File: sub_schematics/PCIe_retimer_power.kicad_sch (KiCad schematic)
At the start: 49 parts

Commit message: Added capacitors
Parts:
- removed C?: C, symbol Device:C
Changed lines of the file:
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@@
 	(wire
 		(pts
-			(xy 31.75 180.34) (xy 21.59 180.34)
-		)
-		(stroke
-			(width 0)
-			(type default)
-		)
-	)
-	(wire
-		(pts
 			(xy 19.05 77.47) (xy 19.05 87.63)
 		)
@@
 	(wire
 		(pts
-			(xy 31.75 167.64) (xy 21.59 167.64)
-		)
-		(stroke
-			(width 0)
-			(type default)
-		)
-	)
-	(wire
-		(pts
 			(xy 115.57 152.4) (xy 115.57 156.21)
 		)
@@
 	(wire
 		(pts
-			(xy 21.59 167.64) (xy 21.59 170.18)
-		)
-		(stroke
-			(width 0)
-			(type default)
-		)
-	)
-	(wire
-		(pts
 			(xy 64.77 154.94) (xy 62.23 154.94)
 		)
@@
 	(wire
 		(pts
-			(xy 21.59 177.8) (xy 21.59 180.34)
-		)
-		(stroke
-			(width 0)
-			(type default)
-		)
-	)
-	(wire
-		(pts
 			(xy 203.2 49.53) (xy 203.2 52.07)
 		)
@@
 					(unit 1)
 				)
-			)
-		)
-	)
-	(symbol
-		(lib_id "Device:C")
-		(at 21.59 173.99 0)
-		(unit 1)
-		(body_style 1)
-		(exclude_from_sim no)
-		(in_bom yes)
-		(on_board yes)
-		(in_pos_files yes)
-		(dnp no)
-		(fields_autoplaced yes)
-		(property "Reference" "C?"
-			(at 25.4 172.7199 0)
-			(show_name no)
-			(do_not_autoplace no)
-			(effects
-				(font
-					(size 1.27 1.27)
-				)
-				(justify left)
-			)
-		)
-		(property "Value" "C"
-			(at 25.4 175.2599 0)
-			(show_name no)
-			(do_not_autoplace no)
-			(effects
-				(font
-					(size 1.27 1.27)
-				)
-				(justify left)
-			)
-		)
-		(property "Footprint" ""
-			(at 22.5552 177.8 0)
-			(hide yes)
-			(show_name no)
-			(do_not_autoplace no)
-			(effects
-				(font
-					(size 1.27 1.27)
-				)
-			)
-		)
-		(property "Datasheet" ""
-			(at 21.59 173.99 0)
-			(hide yes)
-			(show_name no)
-			(do_not_autoplace no)
-			(effects
-				(font
-					(size 1.27 1.27)
-				)
-			)
-		)
-		(property "Description" "Unpolarized capacitor"
-			(at 21.59 173.99 0)
-			(hide yes)
-			(show_name no)
-			(do_not_autoplace no)
-			(effects
-				(font
-					(size 1.27 1.27)
-				)
-			)
-		)
-		(pin "2"
-		)
-		(pin "1"
-		)
-		(instances
-			(project "fw16_MCIO8i"
-				(path "/50f5fd03-67f8-43d1-8bfe-dca2cf908bf0/b129293c-459e-48f0-b955-fe94d8ad35a8/c30304df-3fc6-4616-b0bb-4ddaf654a20e"
-					(reference "C?")
-					(unit 1)
-				)

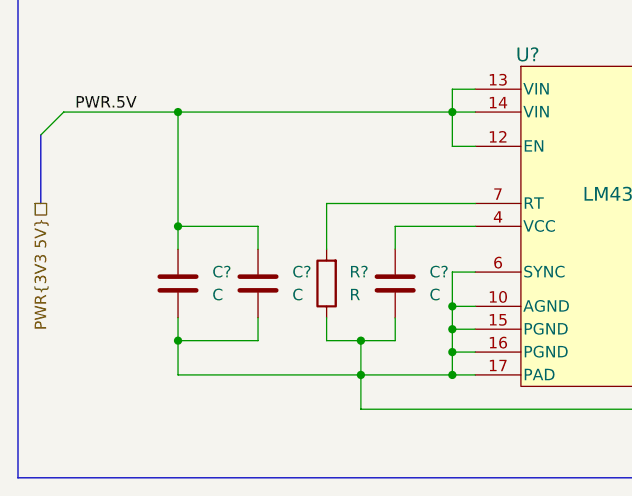
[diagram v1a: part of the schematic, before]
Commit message: Fixed typo
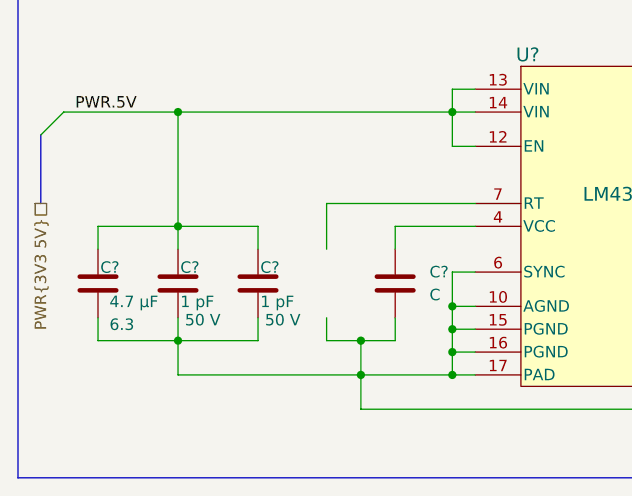
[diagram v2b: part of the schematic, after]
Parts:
- removed C? (x2): C, symbol Device:C
- removed R?: R, symbol Device:R
- added C? (x2): 0402_885392005006, Capacitor_SMD_Wurth:C_Wurth_WCAP-CSRF-0402, symbol WE_WCAP-CSRF:0402_885392005006
- added C?: 0402_885012105008, Capacitor_SMD_Wurth:C_Wurth_WCAP-CSGP-0402, symbol WE_WCAP-CSGP:0402_885012105008
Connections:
- net GND: now also C?.2, C?.2, C?.2
- net PWR.5V: now also C?.1, C?.1, C?.1

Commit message: Working buck converter
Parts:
- removed C? (x20): C, symbol Device:C
- removed C? (x12): C_Polarized_US, symbol Device:C_Polarized_US
- removed L? (x3): L_Small, symbol Device:L_Small
- removed R? (x8): R, symbol Device:R
- added C? (x2): 0402_885012205013, Capacitor_SMD_Wurth:C_Wurth_WCAP-CSGP-0402, symbol WE_WCAP-CSGP:0402_885012205013
- added C? (x10): 1206_H1.6_885012108012, Capacitor_SMD_Wurth:C_Wurth_WCAP-CSGP-1206_H1.6, symbol WE_WCAP-CSGP:1206_H1.6_885012108012
- added C? (x2): 1210_H2.0_885012209005, Capacitor_SMD_Wurth:C_Wurth_WCAP-CSGP-1210_H2.0, symbol WE_WCAP-CSGP:1210_H2.0_885012209005
- added C?: 0603_R_885012006001, Capacitor_SMD_Wurth:C_Wurth_WCAP-CSGP-0603_R, symbol WE_WCAP-CSGP:0603_R_885012006001
- added C? (x4): 1206_H0.8_885012008001, Capacitor_SMD_Wurth:C_Wurth_WCAP-CSGP-1206_H0.8, symbol WE_WCAP-CSGP:1206_H0.8_885012008001
- added C?: 1210_H1.25_885012209003, Capacitor_SMD_Wurth:C_Wurth_WCAP-CSGP-1210_H1.25, symbol WE_WCAP-CSGP:1210_H1.25_885012209003
- added C? (x2): 0402_885012205018, Capacitor_SMD_Wurth:C_Wurth_WCAP-CSGP-0402, symbol WE_WCAP-CSGP:0402_885012205018
- added C?: 0603_R_885012106004, Capacitor_SMD_Wurth:C_Wurth_WCAP-CSGP-0603_R, symbol WE_WCAP-CSGP:0603_R_885012106004
- added C?: 0201_885392004008, Capacitor_SMD_Wurth:C_Wurth_WCAP-CSRF-0201, symbol WE_WCAP-CSRF:0201_885392004008
- added C? (x2): 0201_885012104002, Capacitor_SMD_Wurth:C_Wurth_WCAP-CSGP-0201, symbol WE_WCAP-CSGP:0201_885012104002
- added C? (x2): L7.3W4.3H1.9_875046219001, resistor_rf_alu:CP_Wurth_WCAP-PHSE-L7.3W4.3H1.9, symbol WE_WCAP-PHSE:L7.3W4.3H1.9_875046219001
- added C?: 0402_885012205017, Capacitor_SMD_Wurth:C_Wurth_WCAP-CSGP-0402, symbol WE_WCAP-CSGP:0402_885012205017
- added C?: 0402_885012105004, Capacitor_SMD_Wurth:C_Wurth_WCAP-CSGP-0402, symbol WE_WCAP-CSGP:0402_885012105004
- added C?: 0603_R_885012206021, Capacitor_SMD_Wurth:C_Wurth_WCAP-CSGP-0603_R, symbol WE_WCAP-CSGP:0603_R_885012206021
- added L? (x2): 1510_74439370150, Inductor_SMD_Wurth:L_Wurth_WE-XHMI-1510, symbol WE-XHMI:1510_74439370150
- added L?: 353220_74479335329247, Inductor_SMD_Wurth:L_Wurth_WE-PMFI-353220, symbol WE-PMFI:353220_74479335329247
- added R? (x2): 1210_R_560112140002, Resistor_SMD_Wurth:R_Wurth_WRIS-RSKS-1210_R, symbol WE_WRIS-RSKS:1210_R_560112140002
- added R?: 0603_R_560112116028, Resistor_SMD_Wurth:R_Wurth_WRIS-RSKS-0603_R, symbol WE_WRIS-RSKS:0603_R_560112116028
- added R?: 0402_560112110151, Resistor_SMD_Wurth:R_Wurth_WRIS-RSKS-0402, symbol WE_WRIS-RSKS:0402_560112110151
- added R?: 0402_560112110215, Resistor_SMD_Wurth:R_Wurth_WRIS-RSKS-0402, symbol WE_WRIS-RSKS:0402_560112110215
- added R?: 0402_560112110130, Resistor_SMD_Wurth:R_Wurth_WRIS-RSKS-0402, symbol WE_WRIS-RSKS:0402_560112110130
- added R?: 0603_R_560112116076, Resistor_SMD_Wurth:R_Wurth_WRIS-RSKS-0603_R, symbol WE_WRIS-RSKS:0603_R_560112116076
- added R?: 0603_R_560112116074, Resistor_SMD_Wurth:R_Wurth_WRIS-RSKS-0603_R, symbol WE_WRIS-RSKS:0603_R_560112116074
- added R?: 0603_R_560112116007, Resistor_SMD_Wurth:R_Wurth_WRIS-RSKS-0603_R, symbol WE_WRIS-RSKS:0603_R_560112116007
- added R?: 0402_560112110012, Resistor_SMD_Wurth:R_Wurth_WRIS-RSKS-0402, symbol WE_WRIS-RSKS:0402_560112110012
- C?: Voltage 6.3 -> 6.3 V
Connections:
- net GND: now also C?.2, C?.2, C?.2, C?.2, C?.2, C?.2, C?.2, C?.2, C?.2, C?.2, C?.2, C?.2, C?.2, C?.2, C?.2, C?.2, C?.2, C?.2, C?.2, C?.2, C?.2, R?.1, R?.1, R?.1, R?.2, R?.2, R?.2
- net PWR.1_17V: now also C?.1, C?.1, C?.1, C?.1, C?.1, C?.1, C?.1, C?.1, C?.1, C?.1, C?.1, C?.1, C?.1, C?.1, L?.2, L?.2, R?.1
- net PWR.1_8V: now also C?.1, C?.1, C?.1, L?.2, R?.2
- net PWR.5V: now also C?.1, C?.1, C?.1, C?.1, C?.1, C?.1
- net at U?.18 (FB2_SS): now also C?.1
- net at U?.3 (CBOOT): now also C?.1
- net at U?.1 (SW), U?.2 (SW): now also C?.2, L?.1
- net at U?.11 (PG1_MODE): now also R?.1
- net at U?.14 (FB1): now also R?.1
- net at U?.15 (VCC): now also C?.1, R?.2
- net at U?.17 (RT): now also R?.2
- net at U?.19 (VOSNS2_COMP): now also C?.1, R?.1
- net at U?.2 (CB2): now also C?.1
- net at U?.21 (CONFIG): now also R?.2
- net at U?.3 (SW2): now also C?.2, L?.1
- net at U?.5 (SW1): now also C?.2, L?.1
- net at U?.6 (CB1): now also C?.1
- net at U?.9 (FB): now also C?.2, R?.1, R?.2
- net at U?.4 (VCC): now also C?.1
- net at U?.7 (RT): now also R?.2
- new net: C?.1, R?.2
- new net: C?.2, C?.2, C?.2, C?.2, C?.2, C?.2
- new net: R?.1, R?.1
- no-connect marks 0 -> 2

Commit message: Footprint
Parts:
- removed C? (x9): 1206_H1.6_885012108012, Capacitor_SMD_Wurth:C_Wurth_WCAP-CSGP-1206_H1.6, symbol WE_WCAP-CSGP:1206_H1.6_885012108012
- removed C?: 1210_H2.0_885012209005, Capacitor_SMD_Wurth:C_Wurth_WCAP-CSGP-1210_H2.0, symbol WE_WCAP-CSGP:1210_H2.0_885012209005
- removed L? (x2): 1510_74439370150, Inductor_SMD_Wurth:L_Wurth_WE-XHMI-1510, symbol WE-XHMI:1510_74439370150
- removed R? (x2): 1210_R_560112140002, Resistor_SMD_Wurth:R_Wurth_WRIS-RSKS-1210_R, symbol WE_WRIS-RSKS:1210_R_560112140002
- removed R?: 0603_R_560112116076, Resistor_SMD_Wurth:R_Wurth_WRIS-RSKS-0603_R, symbol WE_WRIS-RSKS:0603_R_560112116076
- added C24: 1210_H2.0_885012209005, WE_WCAP-CSGP:C_Wurth_WCAP-CSGP-1210_H2.0, symbol WE_WCAP-CSGP:1210_H2.0_885012209005
- added C26, C27, C28, C29, C30, C31, C32, C33, C34: 1206_H1.6_885012108012, WE_WCAP-CSGP:C_Wurth_WCAP-CSGP-1206_H1.6, symbol WE_WCAP-CSGP:1206_H1.6_885012108012
- added L2, L3: 353220_74479335329210, WE-PMFI:L_Wurth_WE-PMFI-353220, symbol WE-PMFI:353220_74479335329210
- added R1, R20: 0402_560112110019, WE_WRIS-RSKS:R_Wurth_WRIS-RSKS-0402, symbol WE_WRIS-RSKS:0402_560112110019
- added R17: 0603_R_560112116074, WE_WRIS-RSKS:R_Wurth_WRIS-RSKS-0603_R, symbol WE_WRIS-RSKS:0603_R_560112116074
- C1, C12, C13, C14, C15, C16, C21: renamed from C?; footprint Capacitor_SMD_Wurth:C_Wurth_WCAP-CSGP-0402 -> WE_WCAP-CSGP:C_Wurth_WCAP-CSGP-0402
- C10, C8: renamed from C?; footprint Capacitor_SMD_Wurth:C_Wurth_WCAP-CSRF-0402 -> WE_WCAP-CSRF:C_Wurth_WCAP-CSRF-0402
- C11: renamed from C?; footprint Capacitor_SMD_Wurth:C_Wurth_WCAP-CSGP-0603_R -> WE_WCAP-CSGP:C_Wurth_WCAP-CSGP-0603_R; Voltage 6.3 -> 6.3 V
- C17, C19: renamed from C?; footprint Capacitor_SMD_Wurth:C_Wurth_WCAP-CSGP-0603_R -> WE_WCAP-CSGP:C_Wurth_WCAP-CSGP-0603_R
- C18: renamed from C?; footprint Capacitor_SMD_Wurth:C_Wurth_WCAP-CSRF-0201 -> WE_WCAP-CSRF:C_Wurth_WCAP-CSRF-0201; Voltage 25 -> 25 V
- C2, C3: renamed from C?; footprint Capacitor_SMD_Wurth:C_Wurth_WCAP-CSGP-0201 -> WE_WCAP-CSGP:C_Wurth_WCAP-CSGP-0201
- C20, C22: renamed from C?; footprint resistor_rf_alu:CP_Wurth_WCAP-PHSE-L7.3W4.3H1.9 -> WE_WCAP-PHSE:CP_Wurth_WCAP-PHSE-L7.3W4.3H1.9
- C23: renamed from C?; footprint Capacitor_SMD_Wurth:C_Wurth_WCAP-CSGP-1210_H2.0 -> WE_WCAP-CSGP:C_Wurth_WCAP-CSGP-1210_H2.0
- C25: renamed from C?; footprint Capacitor_SMD_Wurth:C_Wurth_WCAP-CSGP-1206_H1.6 -> WE_WCAP-CSGP:C_Wurth_WCAP-CSGP-1206_H1.6
- C4, C5, C6, C7: renamed from C?; footprint Capacitor_SMD_Wurth:C_Wurth_WCAP-CSGP-1206_H0.8 -> WE_WCAP-CSGP:C_Wurth_WCAP-CSGP-1206_H0.8
- C9: renamed from C?; footprint Capacitor_SMD_Wurth:C_Wurth_WCAP-CSGP-1210_H1.25 -> WE_WCAP-CSGP:C_Wurth_WCAP-CSGP-1210_H1.25
- L1: renamed from L?; footprint Inductor_SMD_Wurth:L_Wurth_WE-PMFI-353220 -> WE-PMFI:L_Wurth_WE-PMFI-353220
- R11, R12, R16: renamed from R?; footprint Resistor_SMD_Wurth:R_Wurth_WRIS-RSKS-0603_R -> WE_WRIS-RSKS:R_Wurth_WRIS-RSKS-0603_R
- R13, R14, R15, R18: renamed from R?; footprint Resistor_SMD_Wurth:R_Wurth_WRIS-RSKS-0402 -> WE_WRIS-RSKS:R_Wurth_WRIS-RSKS-0402
- gave numbers to parts that had none: 2
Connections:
- net GND: now also C24.2, C26.2, C27.2, C28.2, C29.2, C30.2, C31.2, C32.2, C33.2, C34.2, R20.2
- net PWR.1_17V: now also C24.1, C26.1, C27.1, C28.1, C29.1, C30.1, C31.1, C32.1, C33.1, C34.1, L2.2, L3.2, R20.1
- net at U2.11 (PG1_MODE): now also R1.2
- net at C9.1, U2.15 (VCC): now also R1.1
- net at C14.2, U2.3 (SW2): now also L3.1
- net at C13.2, U2.5 (SW1): now also L2.1
- net at R18.1: now also R17.1
- net at C18.2, R16.1, U3.9 (FB): now also R17.2
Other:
- moved on the sheet: C23, C25

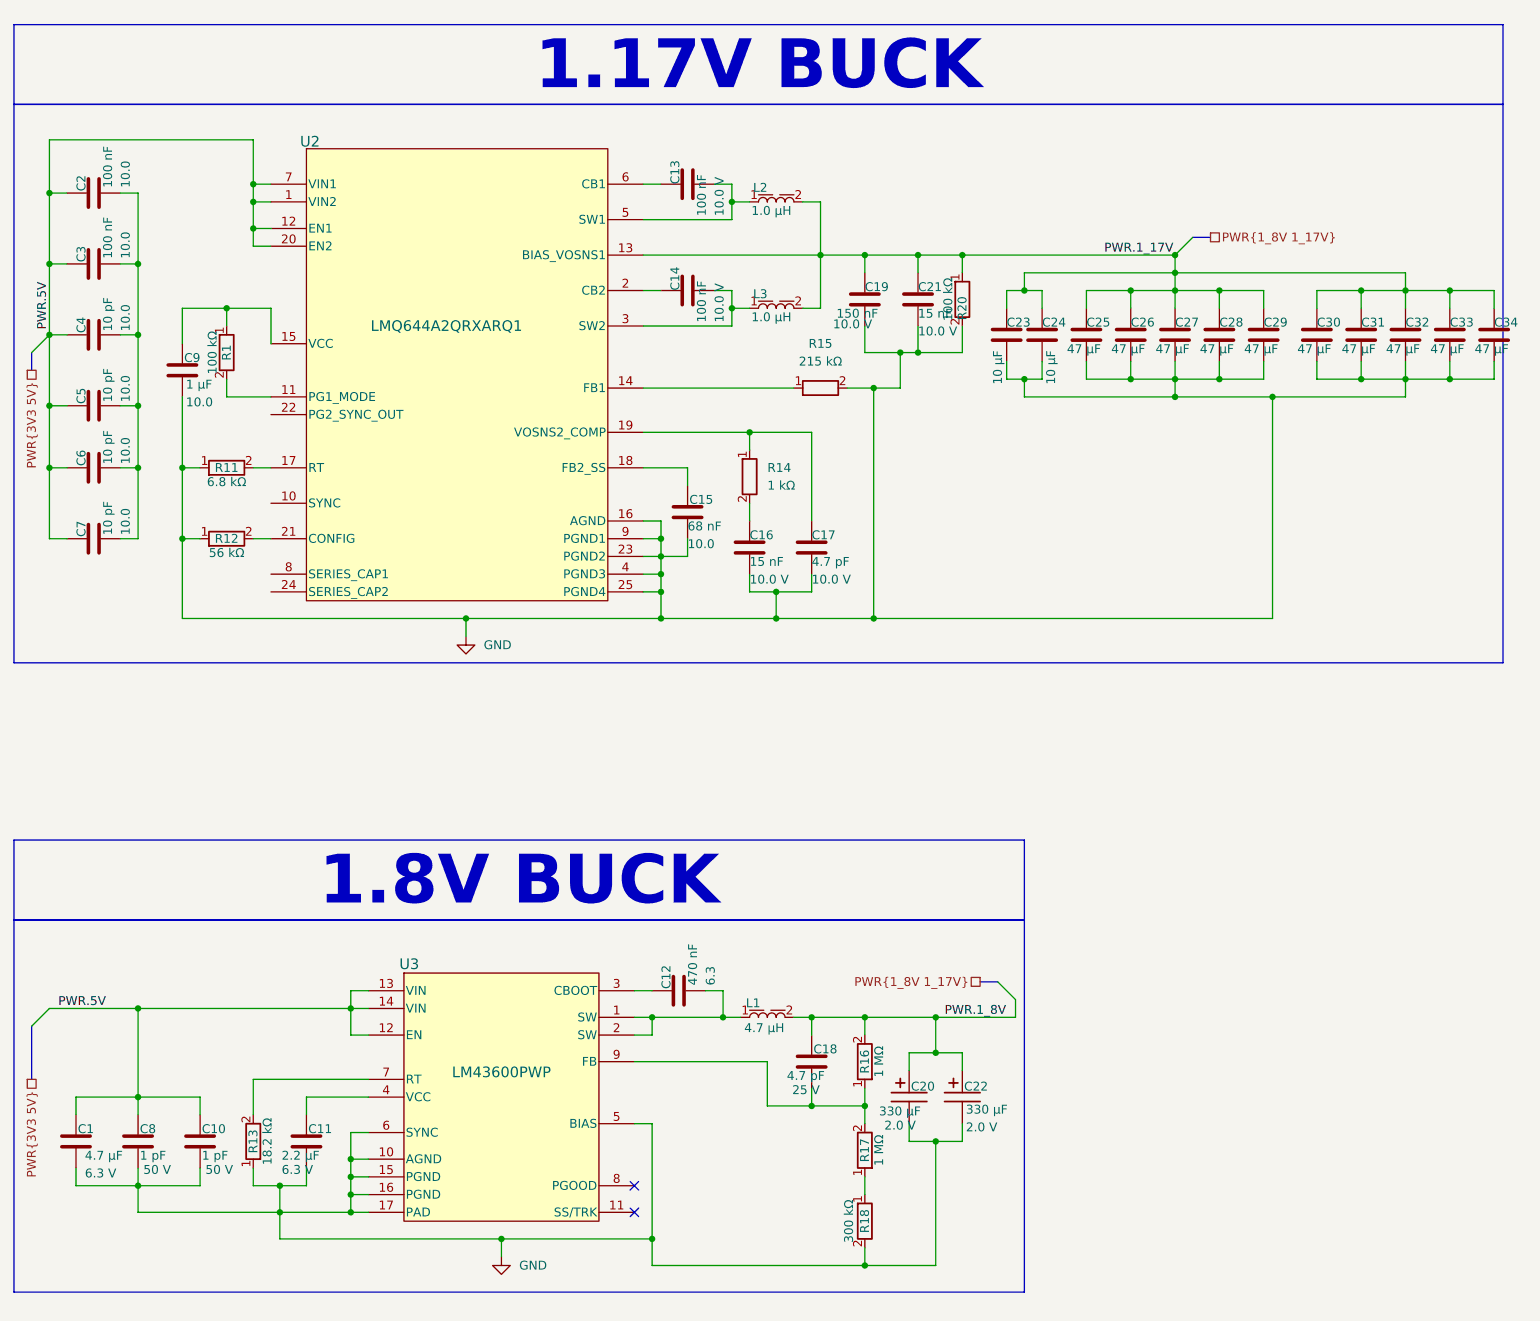
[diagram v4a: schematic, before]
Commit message: changed 1.8V buck
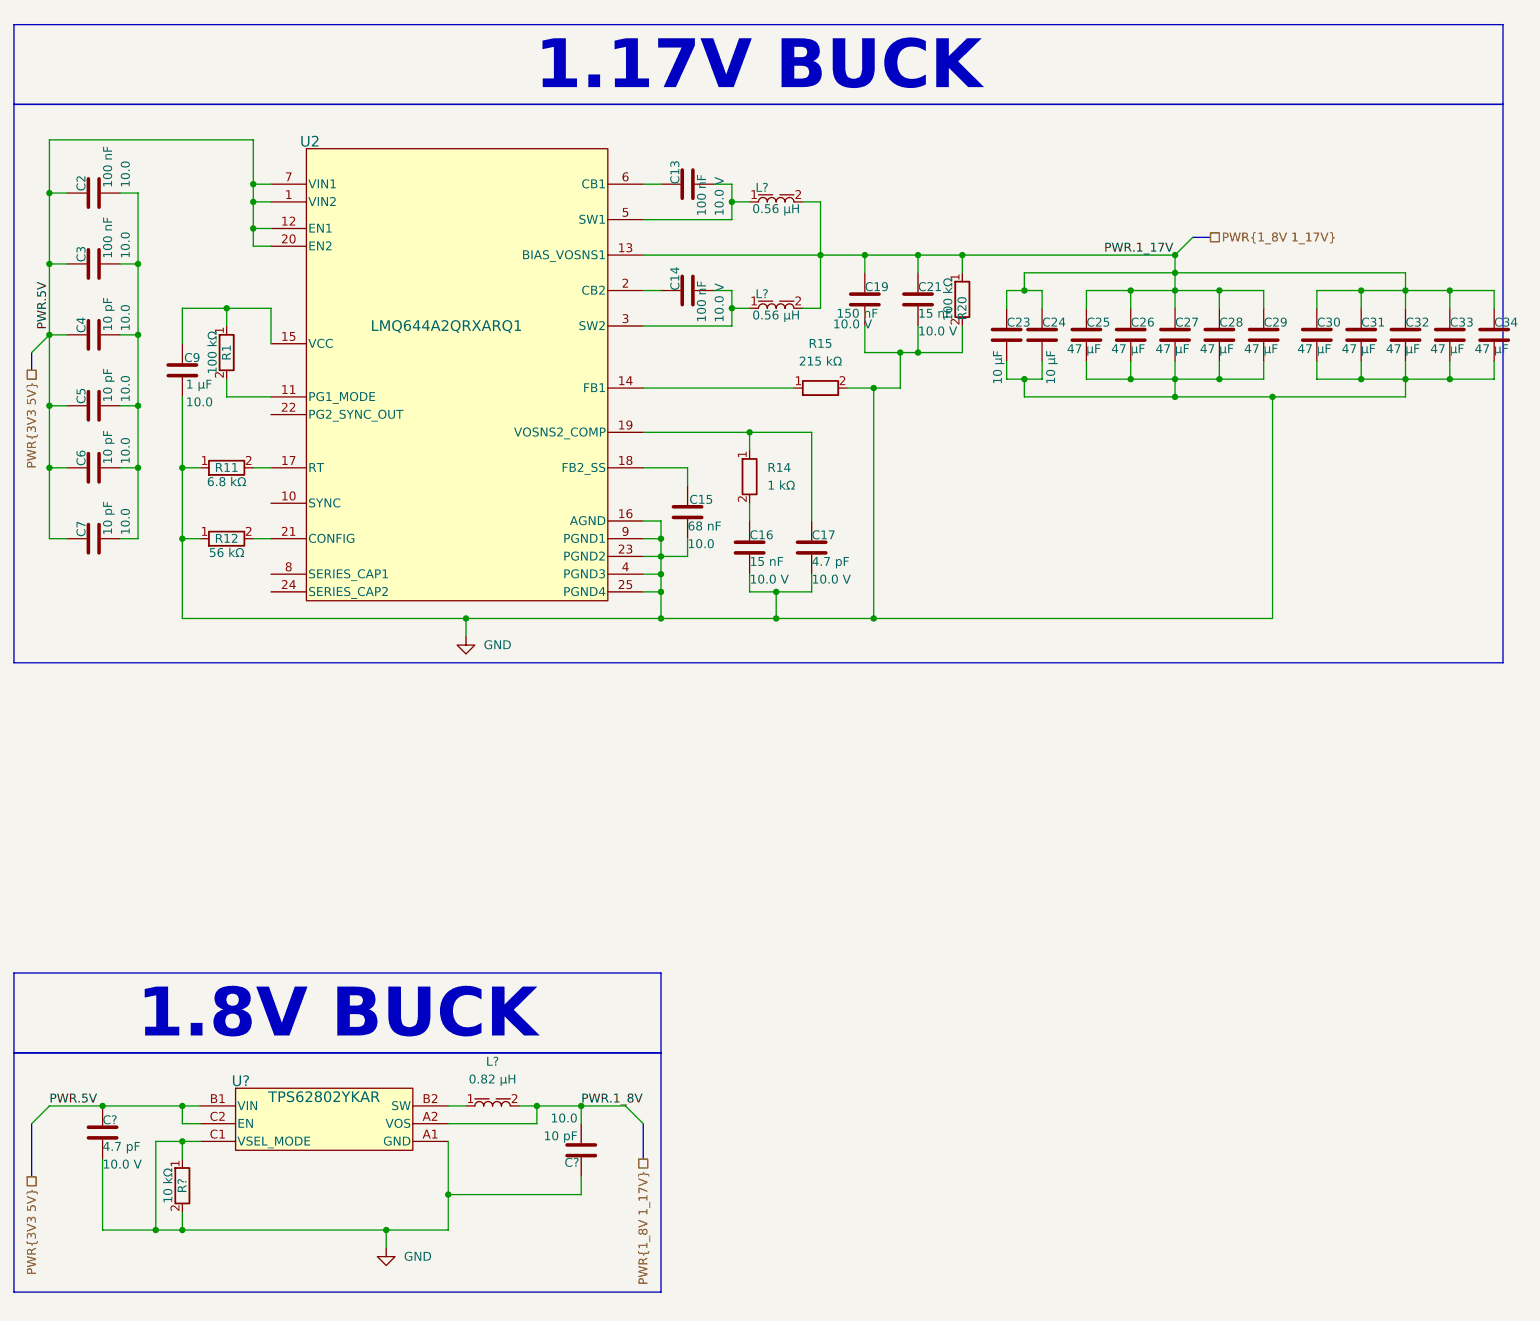
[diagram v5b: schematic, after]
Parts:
- removed C1: 0402_885012105008, WE_WCAP-CSGP:C_Wurth_WCAP-CSGP-0402, symbol WE_WCAP-CSGP:0402_885012105008
- removed C10, C8: 0402_885392005006, WE_WCAP-CSRF:C_Wurth_WCAP-CSRF-0402, symbol WE_WCAP-CSRF:0402_885392005006
- removed C11: 0603_R_885012106004, WE_WCAP-CSGP:C_Wurth_WCAP-CSGP-0603_R, symbol WE_WCAP-CSGP:0603_R_885012106004
- removed C12: 0402_885012105004, WE_WCAP-CSGP:C_Wurth_WCAP-CSGP-0402, symbol WE_WCAP-CSGP:0402_885012105004
- removed C18: 0201_885392004008, WE_WCAP-CSRF:C_Wurth_WCAP-CSRF-0201, symbol WE_WCAP-CSRF:0201_885392004008
- removed C20, C22: L7.3W4.3H1.9_875046219001, WE_WCAP-PHSE:CP_Wurth_WCAP-PHSE-L7.3W4.3H1.9, symbol WE_WCAP-PHSE:L7.3W4.3H1.9_875046219001
- removed L1: 353220_74479335329247, WE-PMFI:L_Wurth_WE-PMFI-353220, symbol WE-PMFI:353220_74479335329247
- removed L2, L3: 353220_74479335329210, WE-PMFI:L_Wurth_WE-PMFI-353220, symbol WE-PMFI:353220_74479335329210
- removed R13: 0402_560112110130, WE_WRIS-RSKS:R_Wurth_WRIS-RSKS-0402, symbol WE_WRIS-RSKS:0402_560112110130
- removed R16, R17: 0603_R_560112116074, WE_WRIS-RSKS:R_Wurth_WRIS-RSKS-0603_R, symbol WE_WRIS-RSKS:0603_R_560112116074
- removed R18: 0402_560112110151, WE_WRIS-RSKS:R_Wurth_WRIS-RSKS-0402, symbol WE_WRIS-RSKS:0402_560112110151
- removed U3: LM43600PWP, step-down-converter-1.8V:PWP0016F, symbol step-down-converter-1.8V:LM43600PWP
- added C?: 0603_R_885012006001, WE_WCAP-CSGP:C_Wurth_WCAP-CSGP-0603_R, symbol WE_WCAP-CSGP:0603_R_885012006001
- added C?: 1206_H0.8_885012008001, WE_WCAP-CSGP:C_Wurth_WCAP-CSGP-1206_H0.8, symbol WE_WCAP-CSGP:1206_H0.8_885012008001
- added L? (x2): 3012_744383340056, WE-MAPI:L_Wurth_WE-MAPI-3012, symbol WE-MAPI:3012_744383340056
- added L?: 1610_744383130082, Inductor_SMD_Wurth:L_Wurth_WE-MAPI-1610, symbol WE-MAPI:1610_744383130082
- added R?: 0402_560112110020, WE_WRIS-RSKS:R_Wurth_WRIS-RSKS-0402, symbol WE_WRIS-RSKS:0402_560112110020
- added U?: TPS62802YKAR, step-down-converter-1.8V:YKA0006ACAC, symbol step-down-converter-1.8V:TPS62802YKAR
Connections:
- net GND: now also C?.1, C?.2, R?.1, R?.2, U?.A1 (GND), U?.C1 (VSEL_MODE)
- net PWR.1_17V: now also L?.2, L?.2
- net PWR.1_8V: now also C?.2, L?.2, U?.A2 (VOS)
- net PWR.5V: now also C?.1, U?.B1 (VIN), U?.C2 (EN)
- net at C14.2, U2.3 (SW2): now also L?.1
- net at C13.2, U2.5 (SW1): now also L?.1
- new net: L?.1, U?.B2 (SW)
- no-connect marks 2 -> 0
